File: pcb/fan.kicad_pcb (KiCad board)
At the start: 2 copper layers, 211.5 x 143.8 mm, 69 parts, among them J1 MJ-4PP-9, SW1 SW_PUSH-kbd, SW10 SW_PUSH-kbd, SW11 SW_PUSH-kbd, SW12 SW_PUSH-kbd, SW13 SW_PUSH-kbd, SW14 SW_PUSH-kbd, SW15 SW_PUSH-kbd, SW16 SW_PUSH-kbd, SW17 SW_PUSH-kbd, SW18 SW_PUSH-kbd, SW19 SW_PUSH-kbd, SW2 SW_PUSH-kbd, SW20 SW_PUSH-kbd, SW21 SW_PUSH-kbd, SW22 SW_PUSH-kbd, SW23 SW_PUSH-kbd, SW24 SW_PUSH-kbd, SW25 SW_PUSH-kbd, SW26 SW_PUSH-kbd, SW27 SW_PUSH-kbd, SW28 SW_PUSH-kbd, SW29 SW_PUSH-kbd, SW3 SW_PUSH-kbd, SW30 SW_PUSH-kbd, SW31 SW_PUSH-kbd, SW32 SW_PUSH-kbd, SW33 SW_PUSH-kbd, SW34 SW_PUSH-kbd, SW35 SW_PUSH-kbd, SW36 SW_PUSH-kbd, SW37 SW_PUSH-kbd, SW38 SW_PUSH-kbd, SW39 SW_PUSH-kbd, SW4 SW_PUSH-kbd, SW40 SW_PUSH-kbd, SW41 SW_PUSH, SW42 SW_PUSH, SW5 SW_PUSH-kbd, SW6 SW_PUSH-kbd, SW7 SW_PUSH-kbd, SW8 SW_PUSH-kbd, SW9 SW_PUSH-kbd, U1 ProMicro, U2 ProMicro, U3 74HC595, U5 74HC595

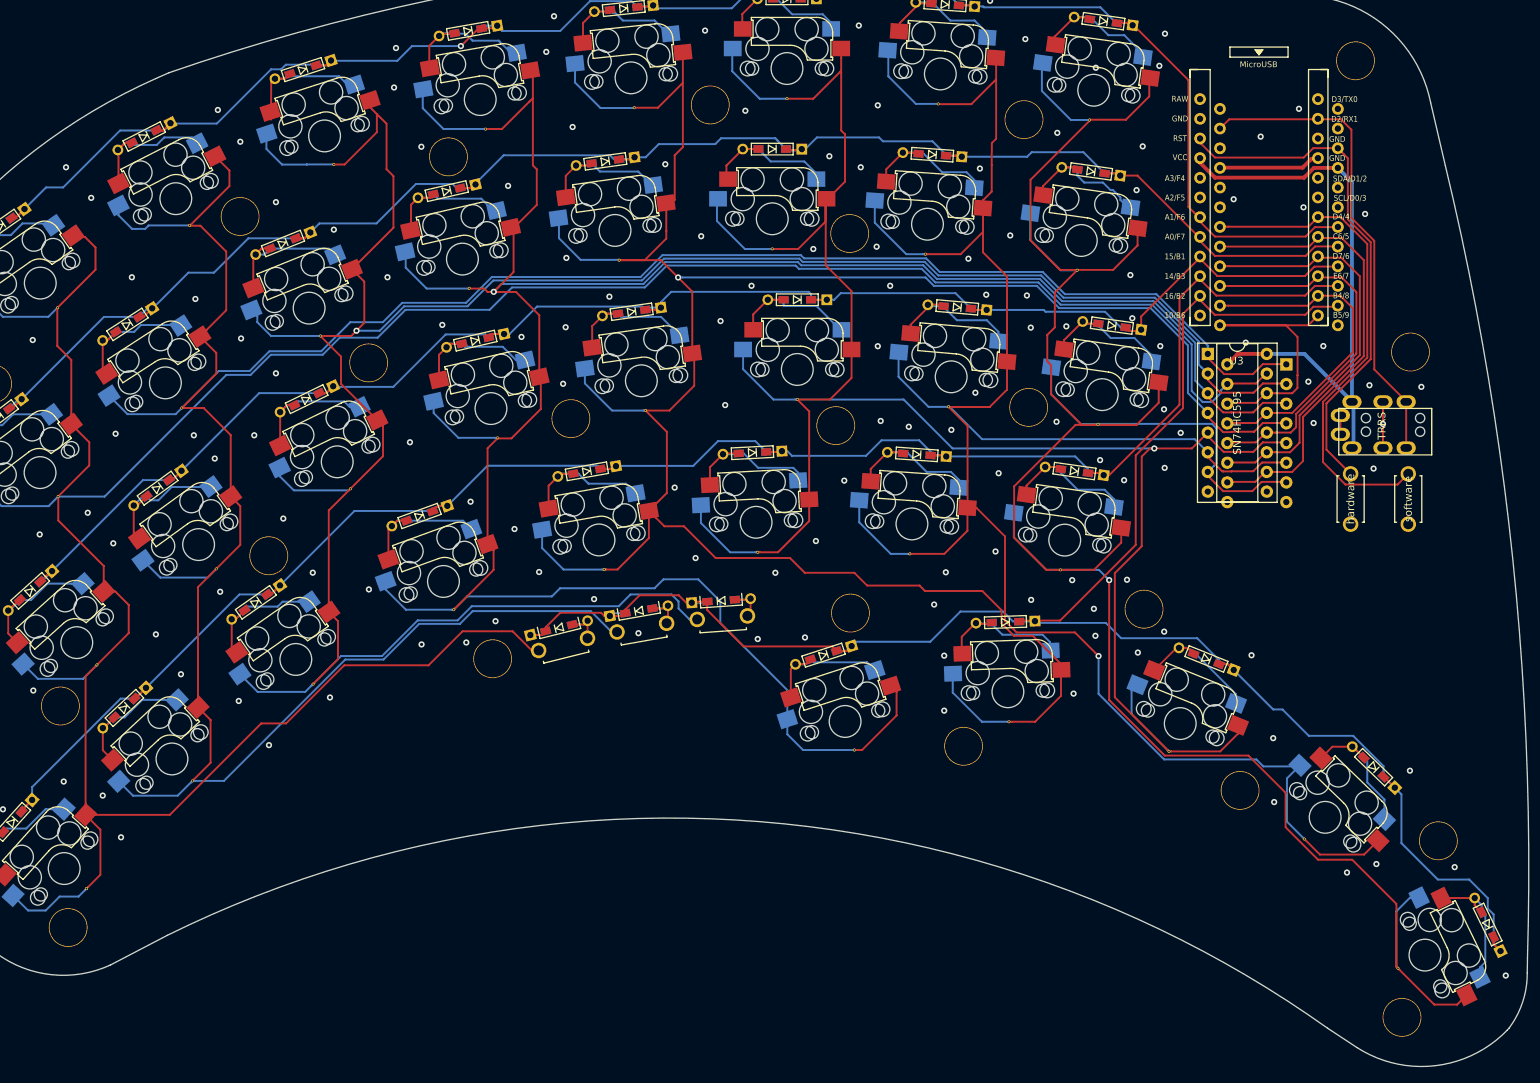
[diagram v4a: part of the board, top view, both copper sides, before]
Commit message: fan74をbluepillに変更
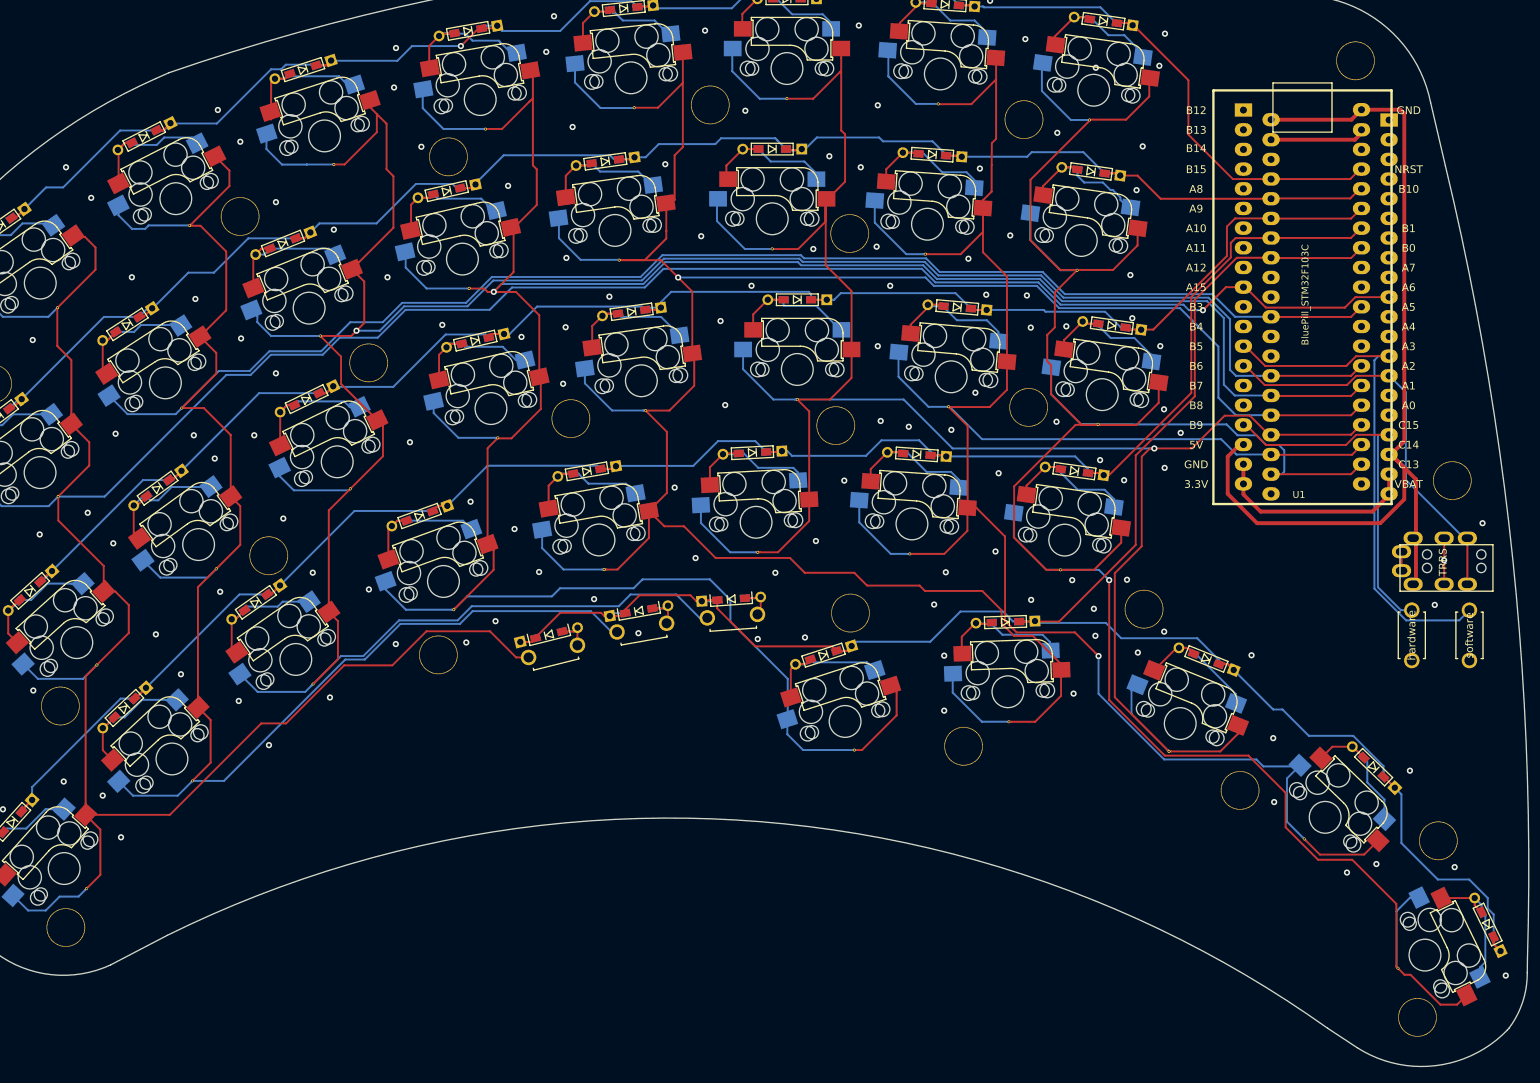
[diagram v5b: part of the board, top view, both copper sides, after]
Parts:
- removed the Ref** at (225.7, 64.2)
- removed the Ref** at (107.2, 103.8)
- removed the Ref** at (224.6, 150.1)
- removed the Ref** at (52.4, 138.5)
- removed U3, U5: 74HC595, kbd:SN74HC595_DIP-16_W7.62mm_Socket_2
- added Ref**: Val**, kbd:HOLE, F.Cu at (231.1, 80.8)
- added Ref**: Val**, kbd:HOLE, F.Cu at (100.2, 103.3)
- added Ref**: Val**, kbd:HOLE, F.Cu at (226.6, 150.1)
- added Ref**: Val**, kbd:HOLE, F.Cu at (52.1, 138.5)
- U1, U2: value ProMicro -> BluePill_STM32F103C; footprint kbd:ProMicro_v3.6 -> BluePill_breakouts:BluePill_STM32F103C
- moved SW41 19.3 mm to (233.3, 100.8)
- moved SW42 19.3 mm to (225.9, 100.8)
- moved J1 19.3 mm to (236.3, 92.1)
- moved U2 19.3 mm to (222.9, 34.3)
- moved U1 13.2 mm to (204.1, 33.0)
- moved SW5 1.58 mm to (115.0, 102.8)
- moved SW15 1.32 mm to (138.2, 98.3)
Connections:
- SW42 pad 2: GND -> (no net)
- U1 pad 10: RCK -> col00
- U1 pad 11: OE -> (no net)
- U1 pad 12: SER -> (no net)
- U1 pad 13: (no net) -> software_reset
- U1 pad 14: row04 -> data
- U1 pad 15: row03 -> (no net)
- U1 pad 16: row02 -> (no net)
- U1 pad 17: row01 -> hardware_reset
- U1 pad 18: row00 -> VCC
- U1 pad 19: (no net) -> GND
- U1 pad 2: data -> (no net)
- U1 pad 20: (no net) -> GND
- U1 pad 21: VCC -> (no net)
- U1 pad 22: hardware_reset -> col07
- U1 pad 23: GND -> col06
- U1 pad 24: (no net) -> col05
- U1 pad 3: GND -> (no net)
- U1 pad 4: GND -> (no net)
- U1 pad 7: software_reset -> (no net)
- U1 pad 8: SCL -> (no net)
- U1 pad 9: SCK -> (no net)
- U2 pad 10: RCK -> col00
- U2 pad 11: OE -> (no net)
- U2 pad 12: SER -> (no net)
- U2 pad 13: (no net) -> software_reset
- U2 pad 14: row04 -> data
- U2 pad 15: row03 -> (no net)
- U2 pad 16: row02 -> (no net)
- U2 pad 17: row01 -> hardware_reset
- U2 pad 18: row00 -> VCC
- U2 pad 19: (no net) -> GND
- U2 pad 2: data -> (no net)
- U2 pad 20: (no net) -> GND
- U2 pad 21: VCC -> (no net)
- U2 pad 22: hardware_reset -> col07
- U2 pad 23: GND -> col06
- U2 pad 24: (no net) -> col05
- U2 pad 3: GND -> (no net)
- U2 pad 4: GND -> (no net)
- U2 pad 7: software_reset -> (no net)
- U2 pad 8: SCL -> (no net)
- U2 pad 9: SCK -> (no net)
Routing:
- net SCL: track 60.3 -> 0.00 mm
- net SCK: track 54.6 -> 0.00 mm
- net RCK: track 49.3 -> 0.00 mm
- net VCC: track 75.9 -> 121.0 mm
- net OE: track 44.2 -> 0.00 mm
- net SER: track 40.3 -> 0.00 mm
- net GND: track 19.1 -> 45.6 mm, vias 136 -> 126
- net hardware_reset: track 67.0 -> 47.1 mm
- net col03: track 333.0 -> 344.6 mm
- net col02: track 336.0 -> 347.2 mm
- net col05: track 277.2 -> 287.6 mm
- net data: track 62.0 -> 51.7 mm
- net col04: track 319.0 -> 327.8 mm
- net col07: track 310.5 -> 319.3 mm
- net col06: track 279.5 -> 288.1 mm
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
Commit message: 配線にちょっと詰まったのでやり直す
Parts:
- added R1: 10K, keyboard_parts:R_1608_rev2, F.Cu at (226.6, 62.2)
- added R10: 10K, keyboard_parts:R_1608_rev2, F.Cu at (226.6, 68.5)
- added R11: 10K, keyboard_parts:R_1608_rev2, F.Cu at (226.6, 74.9)
- added R12: 10K, keyboard_parts:R_1608_rev2, F.Cu at (221.8, 104.0)
- added R2: 10K, keyboard_parts:R_1608_rev2, F.Cu at (226.6, 64.7)
- added R20: 10K, keyboard_parts:R_1608_rev2, F.Cu at (225.7, 66.0)
- added R3: 10K, keyboard_parts:R_1608_rev2, F.Cu at (226.6, 67.3)
- added R4: 10K, keyboard_parts:R_1608_rev2, F.Cu at (226.6, 69.8)
- added R5: 10K, keyboard_parts:R_1608_rev2, F.Cu at (226.6, 72.3)
- added R6: 10K, keyboard_parts:R_1608_rev2, F.Cu at (226.6, 71.0)
- added R7: 10K, keyboard_parts:R_1608_rev2, F.Cu at (226.6, 73.6)
- added R8: 10K, keyboard_parts:R_1608_rev2, F.Cu at (226.6, 76.2)
- added R9: 10K, keyboard_parts:R_1608_rev2, F.Cu at (226.6, 78.7)
- moved U1 25.1 mm to (211.7, 57.0)
- moved U2 25.1 mm to (215.5, 58.3)
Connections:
- J1 pad B: data -> Tx
- SW41 pad 1: software_reset -> hardware_reset
- SW42 pad 1: hardware_reset -> GND
- SW42 pad 2: (no net) -> Net-(R12-Pad2)
- U1 pad 10: col00 -> col02
- U1 pad 11: (no net) -> col01
- U1 pad 12: (no net) -> PA7_R
- U1 pad 13: software_reset -> PB0_R
- U1 pad 14: data -> PB1_R
- U1 pad 15: (no net) -> PB10_R
- U1 pad 16: (no net) -> PB11_R
- U1 pad 22: col07 -> PB13_R
- U1 pad 23: col06 -> PB14_R
- U1 pad 24: col05 -> PB15_R
- U1 pad 25: col04 -> PA8_R
- U1 pad 26: col03 -> Tx
- U1 pad 27: col02 -> Rx
- U1 pad 30: col01 -> (no net)
- U1 pad 33: row04 -> row00
- U1 pad 34: row03 -> row01
- U1 pad 36: row01 -> row03
- U1 pad 37: row00 -> row04
- U1 pad 5: (no net) -> col07
- U1 pad 6: (no net) -> col06
- U1 pad 7: (no net) -> col05
- U1 pad 8: (no net) -> col04
- U1 pad 9: (no net) -> col03
- U2 pad 10: col00 -> col02
- U2 pad 11: (no net) -> col01
- U2 pad 12: (no net) -> PA7_R
- U2 pad 13: software_reset -> PB0_R
- U2 pad 14: data -> PB1_R
- U2 pad 15: (no net) -> PB10_R
- U2 pad 16: (no net) -> PB11_R
- U2 pad 22: col07 -> PB13_R
- U2 pad 23: col06 -> PB14_R
- U2 pad 24: col05 -> PB15_R
- U2 pad 25: col04 -> PA8_R
- U2 pad 26: col03 -> Tx
- U2 pad 27: col02 -> Rx
- U2 pad 30: col01 -> (no net)
- U2 pad 33: row04 -> row00
- U2 pad 34: row03 -> row01
- U2 pad 36: row01 -> row03
- U2 pad 37: row00 -> row04
- U2 pad 5: (no net) -> col07
- U2 pad 6: (no net) -> col06
- U2 pad 7: (no net) -> col05
- U2 pad 8: (no net) -> col04
- U2 pad 9: (no net) -> col03
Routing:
- net Tx: track 0.00 -> 78.2 mm
- net software_reset: track 66.5 -> 0.00 mm
- net data: track 51.7 -> 0.00 mm
- net row04: track 255.8 -> 219.4 mm, vias 0 -> 1
- net VCC: track 121.0 -> 155.6 mm, vias 0 -> 1
- net row03: track 236.9 -> 203.7 mm, vias 0 -> 1
- net col00: track 401.8 -> 373.1 mm, vias 1 -> 0
- net PA7_R: track 0.00 -> 26.1 mm
- net PB11_R: track 0.00 -> 26.0 mm
- net PB0_R: track 0.00 -> 26.0 mm
- net PB10_R: track 0.00 -> 26.0 mm
- net PB1_R: track 0.00 -> 26.0 mm
- net col05: track 287.6 -> 313.3 mm
- net PA8_R: track 0.00 -> 24.8 mm
- net PB14_R: track 0.00 -> 24.8 mm
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
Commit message: fan74のPCBが一応完成した
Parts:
- removed R1, R12, R2, R20, R3, R4, R5, R6, R7, R8: 10K, keyboard_parts:R_1608_rev2
- removed the Ref** at (168.0, 115.1)
- removed the Ref** at (231.1, 80.8)
- removed the Ref** at (203.7, 120.8)
- removed the Ref** at (191.3, 97.4)
- removed the Ref** at (153.4, 97.9)
- removed the Ref** at (176.4, 71.3)
- removed the Ref** at (135.3, 32.3)
- removed the Ref** at (78.3, 90.5)
- removed the Ref** at (74.6, 46.7)
- removed the Ref** at (42.6, 68.3)
- removed the Ref** at (175.8, 34.2)
- removed the Ref** at (218.6, 26.6)
- removed the Ref** at (117.3, 72.8)
- removed the Ref** at (229.3, 127.3)
- removed the Ref** at (51.4, 109.9)
- removed the Ref** at (100.2, 103.3)
- removed the Ref** at (153.3, 48.9)
- removed the Ref** at (91.2, 65.6)
- removed the Ref** at (151.5, 73.7)
- removed the Ref** at (101.5, 39.0)
- removed the Ref** at (226.6, 150.1)
- removed the Ref** at (52.1, 138.5)
- removed SW42: SW_PUSH, kbd:ResetSW
- added Ref**: Val**, kbd:HOLE, B.Cu at (944.5, 30.3)
- added Ref**: Val**, kbd:HOLE, B.Cu at (994.4, 145.6)
- added Ref**: Val**, kbd:HOLE, B.Cu at (1099.6, 146.0)
- added Ref**: Val**, kbd:HOLE, B.Cu at (933.5, 72.9)
- added Ref**: Val**, kbd:HOLE, B.Cu at (937.6, 110.6)
- added Ref**: Val**, kbd:HOLE, F.Cu at (-143.6, 409.5)
- added Ref**: Val**, kbd:HOLE, F.Cu at (-273.8, 465.0)
- added Ref**: Val**, kbd:HOLE, F.Cu at (-219.2, 362.4)
- added Ref**: Val**, kbd:HOLE, F.Cu at (-139.1, 448.7)
- added Ref**: Val**, kbd:HOLE, F.Cu at (-330.5, 484.7)
- added Ref**: Val**, kbd:HOLE, F.Cu at (-143.6, 496.7)
- added Ref**: Val**, kbd:HOLE, B.Cu at (1131.4, 105.5)
- added Ref**: Val**, kbd:HOLE, F.Cu at (-175.4, 369.0)
- added Ref**: Val**, kbd:HOLE, F.Cu at (-280.6, 369.4)
- added Ref**: Val**, kbd:HOLE, F.Cu at (-204.3, 465.6)
- added Ref**: Val**, kbd:HOLE, F.Cu at (-217.7, 402.7)
- added Ref**: Val**, kbd:HOLE, F.Cu at (-280.4, 411.0)
- added Ref**: Val**, kbd:HOLE, F.Cu at (-337.4, 404.4)
- added Ref**: Val**, kbd:HOLE, F.Cu at (-341.5, 442.1)
- added Ref**: Val**, kbd:HOLE, F.Cu at (15.5, 95.1)
- added Ref**: Val**, kbd:HOLE, F.Cu at (19.6, 57.4)
- added Ref**: Val**, kbd:HOLE, F.Cu at (76.6, 64.0)
- added Ref**: Val**, kbd:HOLE, B.Cu at (1001.2, 50.0)
- added Ref**: Val**, kbd:HOLE, F.Cu at (139.3, 55.7)
- added Ref**: Val**, kbd:HOLE, F.Cu at (152.7, 118.6)
- added Ref**: Val**, kbd:HOLE, F.Cu at (76.4, 22.4)
- added Ref**: Val**, kbd:HOLE, F.Cu at (181.6, 22.0)
- added Ref**: Val**, kbd:HOLE, F.Cu at (213.4, 149.7)
- added Ref**: Val**, kbd:HOLE, F.Cu at (26.5, 137.7)
- added Ref**: Val**, kbd:HOLE, F.Cu at (217.9, 101.7)
- added Ref**: Val**, kbd:HOLE, F.Cu at (137.8, 15.4)
- added Ref**: Val**, kbd:HOLE, F.Cu at (83.2, 118.0)
- added Ref**: Val**, kbd:HOLE, F.Cu at (213.4, 62.5)
- added Ref**: Val**, kbd:HOLE, B.Cu at (1055.8, 152.6)
- added Ref**: Val**, kbd:HOLE, B.Cu at (1070.7, 49.4)
- added Ref**: Val**, kbd:HOLE, B.Cu at (1057.3, 112.3)
- added Ref**: Val**, kbd:HOLE, B.Cu at (1135.9, 66.3)
- added Ref**: Val**, kbd:HOLE, B.Cu at (1131.4, 18.3)
- added Ref**: Val**, kbd:HOLE, B.Cu at (994.6, 104.0)
- moved SW15 109.8 mm to (29.6, 114.8), turned to 228 degrees
- moved SW10 101.4 mm to (25.4, 91.6), turned to 222 degrees
- moved SW5 98.1 mm to (24.0, 66.2), turned to 216 degrees
- moved SW41 54.9 mm to (179.1, 91.8), turned to 350 degrees
- moved J1 35.8 mm to (200.9, 97.3), turned to 260 degrees
- moved R9 24.2 mm to (203.9, 70.1), turned to 170 degrees
- moved R11 23.6 mm to (203.4, 79.1), turned to 170 degrees
- moved R10 22.5 mm to (204.5, 72.8), turned to 170 degrees
- moved U2 20.4 mm to (195.3, 60.8), turned to 170 degrees
- moved U1 20.0 mm to (191.8, 58.9), turned to 350 degrees
- moved SW40 17.8 mm to (210.0, 139.5)
- moved SW29 17.8 mm to (123.6, 83.6)
- moved SW12 17.8 mm to (65.9, 56.0)
- moved SW21 17.8 mm to (107.5, 26.2)
- moved SW17 17.8 mm to (85.7, 49.6)
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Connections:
- R9 pad 1: VCC -> Tx
- R9 pad 2: PB13_R -> Rx
- U1 pad 11: col01 -> col03
- U1 pad 12: PA7_R -> col00
- U1 pad 13: PB0_R -> col04
- U1 pad 14: PB1_R -> col05
- U1 pad 15: PB10_R -> (no net)
- U1 pad 16: PB11_R -> (no net)
- U1 pad 22: PB13_R -> (no net)
- U1 pad 23: PB14_R -> (no net)
- U1 pad 24: PB15_R -> (no net)
- U1 pad 25: PA8_R -> (no net)
- U1 pad 33: row00 -> row04
- U1 pad 34: row01 -> row03
- U1 pad 36: row03 -> row01
- U1 pad 37: row04 -> row00
- U1 pad 7: col05 -> (no net)
- U1 pad 8: col04 -> (no net)
- U1 pad 9: col03 -> col01
- U2 pad 11: col01 -> col03
- U2 pad 12: PA7_R -> col00
- U2 pad 13: PB0_R -> col04
- U2 pad 14: PB1_R -> col05
- U2 pad 15: PB10_R -> (no net)
- U2 pad 16: PB11_R -> (no net)
- U2 pad 22: PB13_R -> (no net)
- U2 pad 23: PB14_R -> (no net)
- U2 pad 24: PB15_R -> (no net)
- U2 pad 25: PA8_R -> (no net)
- U2 pad 33: row00 -> row04
- U2 pad 34: row01 -> row03
- U2 pad 36: row03 -> row01
- U2 pad 37: row04 -> row00
- U2 pad 7: col05 -> (no net)
- U2 pad 8: col04 -> (no net)
- U2 pad 9: col03 -> col01
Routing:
- net row04: track 219.4 -> 427.2 mm
- net col01: track 390.5 -> 334.7 mm, vias 0 -> 1
- net row03: track 203.7 -> 236.0 mm
- net col00: track 373.1 -> 345.7 mm
- net PA7_R: track 26.1 -> 0.00 mm
- net PB11_R: track 26.0 -> 0.00 mm
- net PB0_R: track 26.0 -> 0.00 mm
- net PB10_R: track 26.0 -> 0.00 mm
- net PB1_R: track 26.0 -> 0.00 mm
- net PA8_R: track 24.8 -> 0.00 mm
- net PB14_R: track 24.8 -> 0.00 mm
- net PB15_R: track 24.8 -> 0.00 mm
- net PB13_R: track 24.8 -> 0.00 mm
- net col02: track 358.7 -> 334.2 mm
- net col05: track 313.3 -> 290.6 mm
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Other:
- board size 211.5 x 143.8 mm -> 706.1 x 736.6 mm
- board text added: "Fan74 v1.0 Designed by @xcd0 20200314"
